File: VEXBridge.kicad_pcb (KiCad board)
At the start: 2 copper layers, 30 x 40 mm, 37 parts, among them J1 4P4C, J3 Conn_01x05_Pin, U1 LM2596S-5, U2 MAX481E, U5 SN74LVC2G14DBV

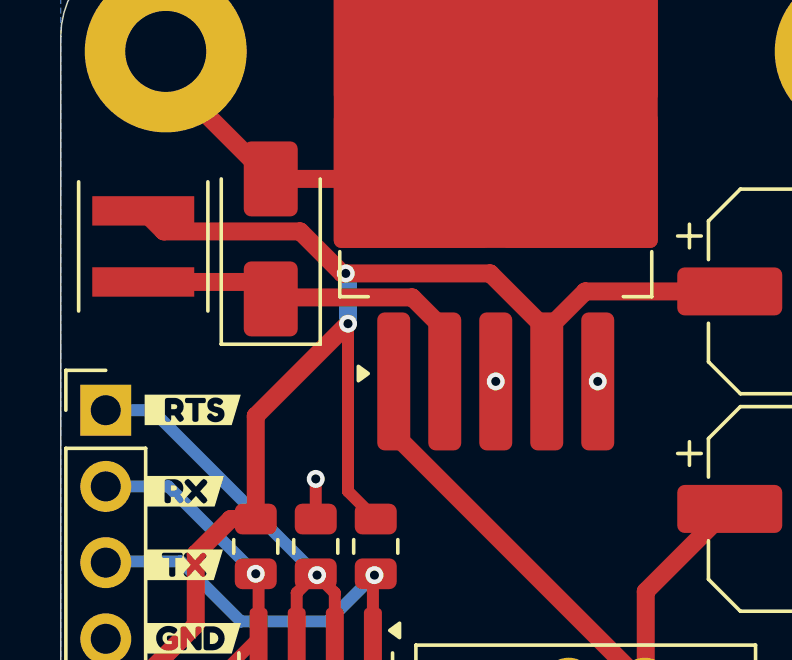
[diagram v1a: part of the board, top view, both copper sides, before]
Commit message: Increased Inductor Footprint
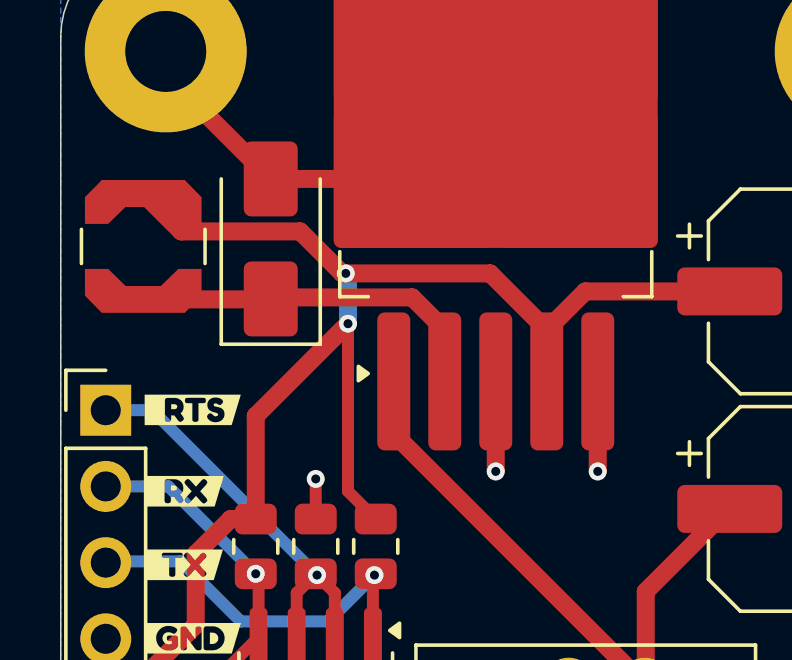
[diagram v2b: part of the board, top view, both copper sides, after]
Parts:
- L1: footprint Inductor_SMD:L_Coilcraft_XxL4020 -> Inductor_SMD:L_Coilcraft_LPS4018
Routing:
- net GND: track 46.9 -> 52.9 mm
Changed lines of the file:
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@@
 		)
 	)
-	(footprint "Inductor_SMD:L_Coilcraft_XxL4020"
+	(footprint "Inductor_SMD:L_Coilcraft_LPS4018"
 		(layer "F.Cu")
 		(at 87.75 65 90)
-		(descr "L_Coilcraft_XxL4020 https://www.coilcraft.com/pdfs/xfl4020.pdf")
-		(tags "L Coilcraft XxL4020")
+		(descr "SMD Inductor Coilcraft LPS4018 https://www.coilcraft.com/pdfs/lps4018.pdf")
+		(tags "L Coilcraft LPS4018")
 		(property "Reference" "L1"
-			(at 3.5 0 90)
+			(at 0 -3 90)
 			(layer "F.SilkS")
 			(hide yes)
@@
 		)
 		(property "Value" "47uH"
-			(at 1 -3 90)
+			(at 0 3 90)
 			(layer "F.Fab")
 			(hide yes)
@@
 			)
 		)
-		(property "Footprint" "Inductor_SMD:L_Coilcraft_XxL4020"
+		(property "Footprint" "Inductor_SMD:L_Coilcraft_LPS4018"
 			(at 0 0 90)
 			(unlocked yes)
@@
 		(attr smd)
 		(fp_line
-			(start -2.154 -2.154)
-			(end 2.154 -2.154)
+			(start -0.57 -2.06)
+			(end 0.57 -2.06)
 			(stroke
 				(width 0.12)
@@
 		)
 		(fp_line
-			(start 2.154 2.154)
-			(end -2.154 2.154)
+			(start -0.57 2.06)
+			(end 0.57 2.06)
 			(stroke
 				(width 0.12)
@@
 		)
 		(fp_line
-			(start 2.26 -2.26)
-			(end 2.26 2.26)
+			(start 1.75 -2.2)
+			(end 2.45 -1.5)
 			(stroke
 				(width 0.05)
@@
 		)
 		(fp_line
-			(start -2.26 -2.26)
-			(end 2.26 -2.26)
+			(start -1.75 -2.2)
+			(end 1.75 -2.2)
 			(stroke
 				(width 0.05)
@@
 		)
 		(fp_line
-			(start 2.26 2.26)
-			(end -2.26 2.26)
+			(start -1.75 -2.2)
+			(end -2.45 -1.5)
 			(stroke
 				(width 0.05)
@@
 		)
 		(fp_line
-			(start -2.26 2.26)
-			(end -2.26 -2.26)
+			(start 2.45 -1.5)
+			(end 2.45 1.5)
 			(stroke
 				(width 0.05)
@@
 		)
 		(fp_line
-			(start 2 -2)
-			(end 2 2)
+			(start -2.45 -1.5)
+			(end -2.45 1.5)
+			(stroke
+				(width 0.05)
+				(type solid)
+			)
+			(layer "F.CrtYd")
+		)
+		(fp_line
+			(start 1.75 2.2)
+			(end 2.45 1.5)
+			(stroke
+				(width 0.05)
+				(type solid)
+			)
+			(layer "F.CrtYd")
+		)
+		(fp_line
+			(start -1.75 2.2)
+			(end -2.45 1.5)
+			(stroke
+				(width 0.05)
+				(type solid)
+			)
+			(layer "F.CrtYd")
+		)
+		(fp_line
+			(start -1.75 2.2)
+			(end 1.75 2.2)
+			(stroke
+				(width 0.05)
+				(type solid)
+			)
+			(layer "F.CrtYd")
+		)
+		(fp_line
+			(start 1.2 -1.95)
+			(end 1.95 -1.2)
 			(stroke
 				(width 0.1)
@@
 		)
 		(fp_line
-			(start -2 -2)
-			(end 2 -2)
+			(start -1.2 -1.95)
+			(end 1.2 -1.95)
 			(stroke
 				(width 0.1)
@@
 		)
 		(fp_line
-			(start 2 2)
-			(end -2 2)
+			(start 1.95 -1.2)
+			(end 1.95 1.2)
 			(stroke
 				(width 0.1)
@@
 		)
 		(fp_line
-			(start -2 2)
-			(end -2 -2)
+			(start -1.95 -1.2)
+			(end -1.21 -1.95)
+			(stroke
+				(width 0.1)
+				(type solid)
+			)
+			(layer "F.Fab")
+		)
+		(fp_line
+			(start -1.95 1.2)
+			(end -1.95 -1.2)
+			(stroke
+				(width 0.1)
+				(type solid)
+			)
+			(layer "F.Fab")
+		)
+		(fp_line
+			(start -1.95 1.2)
+			(end -1.2 1.95)
+			(stroke
+				(width 0.1)
+				(type solid)
+			)
+			(layer "F.Fab")
+		)
+		(fp_line
+			(start 1.2 1.95)
+			(end 1.95 1.2)
+			(stroke
+				(width 0.1)
+				(type solid)
+			)
+			(layer "F.Fab")
+		)
+		(fp_line
+			(start 1.2 1.95)
+			(end -1.2 1.95)
 			(stroke
 				(width 0.1)
@@
 			(effects
 				(font
-					(size 1 1)
-					(thickness 0.15)
+					(size 0.8 0.8)
+					(thickness 0.12)
 				)
 			)
 		)
-		(pad "1" smd rect
-			(at -1.185 0 90)
-			(size 0.98 3.4)
+		(pad "1" smd custom
+			(at -1.765 0 90)
+			(size 0.87 2.79)
 			(layers "F.Cu" "F.Paste" "F.Mask")
 			(net 11 "Net-(D9-K)")
 			(pinfunction "1")
 			(pintype "passive")
+			(zone_connect 2)
+			(options
+				(clearance outline)
+				(anchor rect)
+			)
+			(primitives
+				(gr_poly
+					(pts
+						(xy 1.015 -1.17) (xy 0.435 -0.575) (xy 0.435 0.575) (xy 1.015 1.17) (xy 1.015 1.945) (xy 0.125 1.945)
+						(xy -0.435 1.395) (xy -0.435 -1.395) (xy 0.125 -1.945) (xy 1.015 -1.945)
+					)
+					(width 0)
+					(fill yes)
+				)
+			)
 		)
-		(pad "2" smd rect
-			(at 1.185 0 90)
-			(size 0.98 3.4)
+		(pad "2" smd custom
+			(at 1.765 0 90)
+			(size 0.87 2.79)
 			(layers "F.Cu" "F.Paste" "F.Mask")
 			(net 3 "+5V")
 			(pinfunction "2")
 			(pintype "passive")
+			(zone_connect 2)
+			(options
+				(clearance outline)
+				(anchor rect)
+			)
+			(primitives
+				(gr_poly
+					(pts
+						(xy 0.435 -1.395) (xy 0.435 1.395) (xy -0.125 1.945) (xy -1.015 1.945) (xy -1.015 1.17) (xy -0.435 0.575)
+						(xy -0.435 -0.575) (xy -1.015 -1.17) (xy -1.015 -1.945) (xy -0.125 -1.945)
+					)
+					(width 0)
+					(fill yes)
+				)
+			)
 		)
-		(model "${KICAD8_3DMODEL_DIR}/Inductor_SMD.3dshapes/L_Coilcraft_XxL4020.wrl"
+		(model "${KICAD8_3DMODEL_DIR}/Inductor_SMD.3dshapes/L_Coilcraft_LPS4018.wrl"
 			(offset
 				(xyz 0 0 0)
@@
 	)
 	(segment
+		(start 102.9 72.5)
+		(end 102.9 69.5)
+		(width 0.6)
+		(layer "F.Cu")
+		(net 1)
+	)
+	(segment
 		(start 88.5 58.5)
 		(end 88.5 59.25)
@@
 	)
 	(segment
+		(start 99.5 69.5)
+		(end 99.5 72.5)
+		(width 0.6)
+		(layer "F.Cu")
+		(net 1)
+	)
+	(segment
 		(start 110.5 90.5)
 		(end 111.5 91.5)
@@
 	)
 	(via
-		(at 99.5 69.5)
+		(at 99.5 72.5)
 		(size 0.6)
 		(drill 0.3)
@@
 	)
 	(via
-		(at 102.9 69.5)
+		(at 102.9 72.5)
 		(size 0.6)
 		(drill 0.3)
@@
 	)
 	(segment
-		(start 94.382412 65.9)
-		(end 92.982412 64.5)
-		(width 0.6)
-		(layer "F.Cu")
-		(net 3)
-	)
-	(segment
 		(start 95.5125 86.1)
 		(end 109.525 86.1)
@@
 	)
 	(segment
+		(start 89.015 64.5)
+		(end 87.75 63.235)
+		(width 0.6)
+		(layer "F.Cu")
+		(net 3)
+	)
+	(segment
 		(start 89.225001 84.75)
 		(end 88.75 85.225001)
@@
 	)
 	(segment
-		(start 88.435 64.5)
-		(end 87.75 63.815)
-		(width 0.6)
-		(layer "F.Cu")
-		(net 3)
-	)
-	(segment
 		(start 88.75 85.225001)
 		(end 88.75 85.8875)
@@
 	)
 	(segment
-		(start 92.982412 64.5)
-		(end 88.435 64.5)
-		(width 0.6)
-		(layer "F.Cu")
-		(net 3)
-	)
-	(segment
 		(start 94.575 67.575)
 		(end 94.575 73.1625)
@@
 	)
 	(segment
+		(start 92.982412 64.5)
+		(end 89.015 64.5)
+		(width 0.6)
+		(layer "F.Cu")
+		(net 3)
+	)
+	(segment
 		(start 95.73 84.75)
 		(end 95.73 83.3)
@@
 	)
 	(segment
-		(start 87.1 84.35)
-		(end 87.1 84.356974)
-		(width 0.4)
+		(start 94.382412 65.9)
+		(end 92.982412 64.5)
+		(width 0.6)
 		(layer "F.Cu")
 		(net 3)
 	)
 	(segment
-		(start 95.73 85.8575)
-		(end 95.5 86.0875)
+		(start 87.1 84.35)
+		(end 87.1 84.356974)
 		(width 0.4)
 		(layer "F.Cu")
@@
 	)
 	(segment
+		(start 95.73 85.8575)
+		(end 95.5 86.0875)
+		(width 0.4)
+		(layer "F.Cu")
+		(net 3)
+	)
+	(segment
 		(start 99.317588 65.9)
 		(end 101.2 67.782412)
@@
 	)
 	(segment
-		(start 91.435 66.185)
-		(end 92 66.75)
+		(start 92 66.75)
+		(end 92.05 66.7)
 		(width 0.6)
 		(layer "F.Cu")
@@
 	)
 	(segment
-		(start 92 66.75)
-		(end 92.05 66.7)
+		(start 91.985 66.765)
+		(end 92 66.75)
 		(width 0.6)
 		(layer "F.Cu")
@@
 	)
 	(segment
-		(start 96.717588 66.7)
-		(end 97.8 67.782412)
+		(start 87.75 66.765)
+		(end 91.985 66.765)
 		(width 0.6)
 		(layer "F.Cu")
@@
 	)
 	(segment
-		(start 87.75 66.185)
-		(end 91.435 66.185)
+		(start 96.717588 66.7)
+		(end 97.8 67.782412)
 		(width 0.6)
 		(layer "F.Cu")
